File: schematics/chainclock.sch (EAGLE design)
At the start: 19 parts, among them SW1 ROTARTY_ENCODER

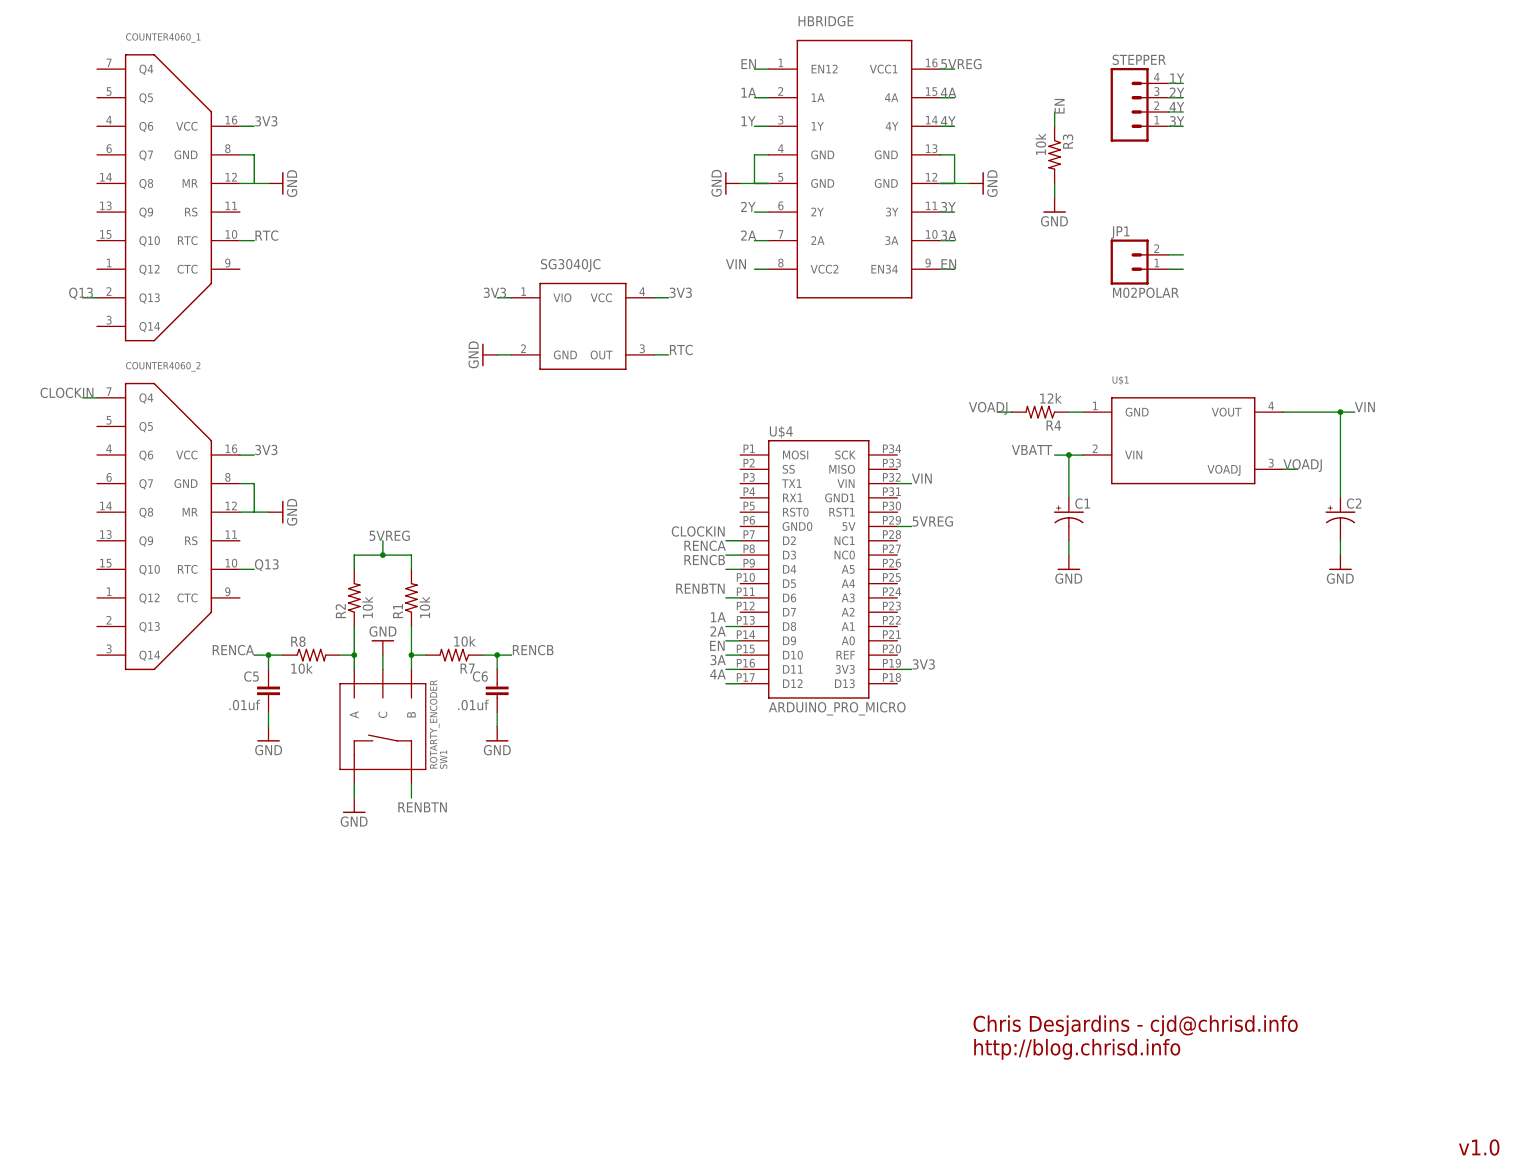
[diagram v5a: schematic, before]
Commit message: Move encoder off board
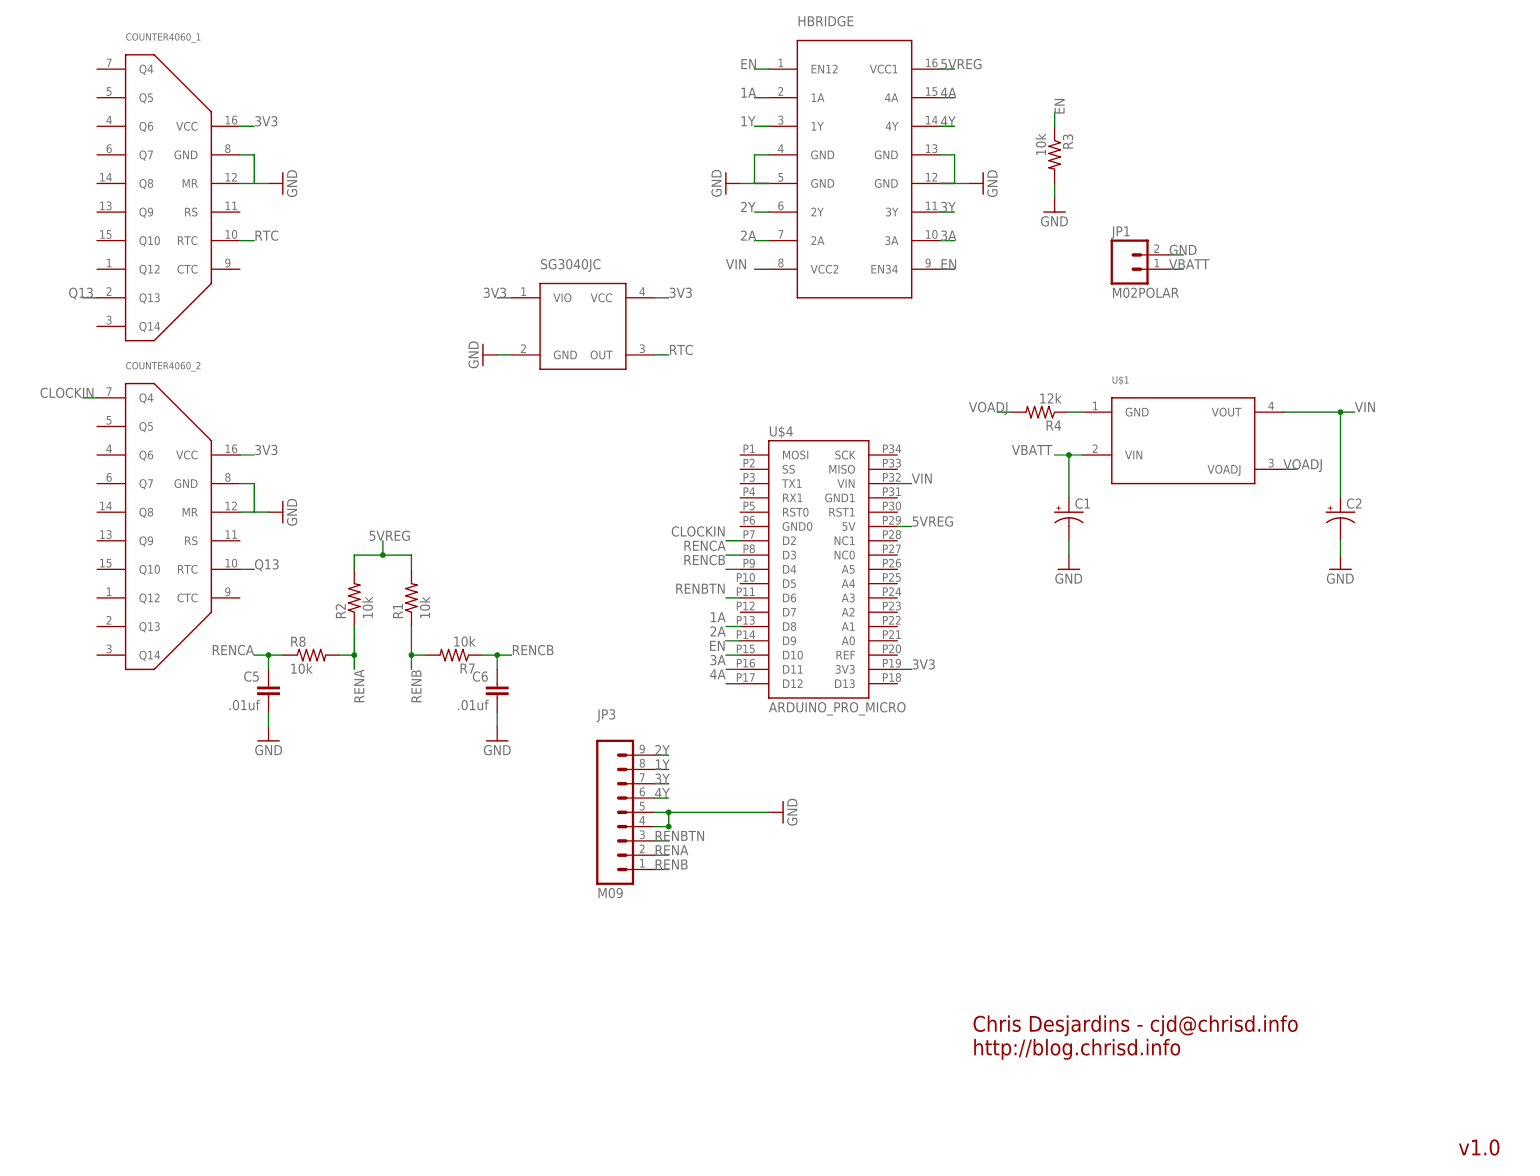
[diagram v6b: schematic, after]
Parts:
- removed STEPPER: (no value), SparkFun-Connectors:M04PTH
- removed SW1: ROTARTY_ENCODER, SparkFun-Electromechanical:ROTARTY_ENCODER
- added JP3: M09, SparkFun-Connectors:M09
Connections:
- removed net N$2: R1.1, R7.2, SW1.B
- removed net N$5: R2.1, R8.2, SW1.A
- new net RENA: JP3.2, R2.1, R8.2
- new net RENB: JP3.1, R1.1, R7.2
- net 1Y: now also JP3.8; no longer STEPPER.4
- net 2Y: now also JP3.9; no longer STEPPER.3
- net 3Y: now also JP3.7; no longer STEPPER.1
- net 4Y: now also JP3.6; no longer STEPPER.2
- net GND: now also JP3.4, JP3.5; no longer SW1.C, SW1.SW-
- net RENBTN: now also JP3.3; no longer SW1.SW+
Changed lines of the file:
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@@
 <part name="GND3" library="SparkFun-Aesthetics" deviceset="GND" device=""/>
 <part name="GND4" library="SparkFun-Aesthetics" deviceset="GND" device=""/>
-<part name="STEPPER" library="SparkFun-Connectors" deviceset="M04" device="PTH"/>
 <part name="R3" library="SparkFun-Resistors" deviceset="RESISTOR" device="EZ" value="10k"/>
 <part name="GND5" library="SparkFun-Aesthetics" deviceset="GND" device=""/>
 <part name="FRAME1" library="frames" deviceset="FRAME_A_L" device=""/>
-<part name="SW1" library="SparkFun-Electromechanical" deviceset="ROTARTY_ENCODER" device=""/>
-<part name="GND7" library="SparkFun-Aesthetics" deviceset="GND" device=""/>
 <part name="C5" library="SparkFun-Capacitors" deviceset="CAP" device="KIT" value=".01uf"/>
 <part name="C6" library="SparkFun-Capacitors" deviceset="CAP" device="KIT" value=".01uf"/>
 <part name="GND10" library="SparkFun-Aesthetics" deviceset="GND" device=""/>
 <part name="GND11" library="SparkFun-Aesthetics" deviceset="GND" device=""/>
-<part name="GND12" library="SparkFun-Aesthetics" deviceset="GND" device=""/>
 <part name="GND1" library="SparkFun-Aesthetics" deviceset="GND" device=""/>
 <part name="SG3040JC" library="desjardins" deviceset="SG30XX" device="JC"/>
@@
 <part name="COUNTER4060_2" library="desjardins" deviceset="4060" device="SOIC16"/>
 <part name="GND2" library="SparkFun-Aesthetics" deviceset="GND" device=""/>
+<part name="JP3" library="SparkFun-Connectors" deviceset="M09" device=""/>
+<part name="GND14" library="SparkFun-Aesthetics" deviceset="GND" device=""/>
 </parts>
 <sheets>
@@
 <instance part="GND3" gate="1" x="132.08" y="180.34" rot="R270"/>
 <instance part="GND4" gate="1" x="177.8" y="180.34" rot="R90"/>
-<instance part="STEPPER" gate="G$1" x="205.74" y="193.04"/>
 <instance part="R3" gate="G$1" x="190.5" y="185.42" rot="R270"/>
 <instance part="GND5" gate="1" x="190.5" y="175.26"/>
 <instance part="FRAME1" gate="G$1" x="0" y="0"/>
 <instance part="FRAME1" gate="G$2" x="172.72" y="0"/>
-<instance part="SW1" gate="G$1" x="71.12" y="83.82" rot="MR90"/>
-<instance part="GND7" gate="1" x="71.12" y="99.06" rot="R180"/>
 <instance part="C5" gate="G$1" x="50.8" y="88.9" rot="MR0"/>
 <instance part="C6" gate="G$1" x="91.44" y="88.9" rot="MR0"/>
 <instance part="GND10" gate="1" x="91.44" y="81.28" rot="MR0"/>
 <instance part="GND11" gate="1" x="50.8" y="81.28" rot="MR0"/>
-<instance part="GND12" gate="1" x="66.04" y="68.58"/>
 <instance part="GND1" gate="1" x="88.9" y="149.86" rot="R270"/>
 <instance part="SG3040JC" gate="G$1" x="106.68" y="154.94"/>
@@
 <instance part="COUNTER4060_2" gate="G$1" x="33.02" y="119.38"/>
 <instance part="GND2" gate="1" x="53.34" y="121.92" rot="R90"/>
+<instance part="JP3" gate="G$1" x="109.22" y="68.58"/>
+<instance part="GND14" gate="1" x="142.24" y="68.58" rot="MR270"/>
 </instances>
 <busses>
@@
 </segment>
 <segment>
-<pinref part="SW1" gate="G$1" pin="C"/>
-<wire x1="71.12" y1="93.98" x2="71.12" y2="96.52" width="0.1524" layer="91"/>
-<pinref part="GND7" gate="1" pin="GND"/>
-</segment>
-<segment>
 <pinref part="C6" gate="G$1" pin="2"/>
 <wire x1="91.44" y1="86.36" x2="91.44" y2="83.82" width="0.1524" layer="91"/>
@@
 </segment>
 <segment>
-<pinref part="SW1" gate="G$1" pin="SW-"/>
-<wire x1="66.04" y1="73.66" x2="66.04" y2="71.12" width="0.1524" layer="91"/>
-<pinref part="GND12" gate="1" pin="GND"/>
-</segment>
-<segment>
 <wire x1="93.98" y1="149.86" x2="91.44" y2="149.86" width="0.1524" layer="91"/>
 <pinref part="GND1" gate="1" pin="GND"/>
@@
 <pinref part="JP1" gate="G$1" pin="2"/>
 <wire x1="210.82" y1="167.64" x2="213.36" y2="167.64" width="0.1524" layer="91"/>
+<label x="210.82" y="167.64" size="1.778" layer="95"/>
 </segment>
 <segment>
@@
 <pinref part="GND2" gate="1" pin="GND"/>
 </segment>
+<segment>
+<pinref part="JP3" gate="G$1" pin="4"/>
+<wire x1="119.38" y1="66.04" x2="121.92" y2="66.04" width="0.1524" layer="91"/>
+<wire x1="121.92" y1="66.04" x2="121.92" y2="68.58" width="0.1524" layer="91"/>
+<pinref part="JP3" gate="G$1" pin="5"/>
+<wire x1="119.38" y1="68.58" x2="121.92" y2="68.58" width="0.1524" layer="91"/>
+<junction x="121.92" y="68.58"/>
+<wire x1="121.92" y1="68.58" x2="139.7" y2="68.58" width="0.1524" layer="91"/>
+<junction x="121.92" y="66.04"/>
+<pinref part="GND14" gate="1" pin="GND"/>
+</segment>
 </net>
 <net name="CLOCKIN" class="0">
@@
 </segment>
 <segment>
-<pinref part="STEPPER" gate="G$1" pin="4"/>
-<wire x1="210.82" y1="198.12" x2="213.36" y2="198.12" width="0.1524" layer="91"/>
-<label x="210.82" y="198.12" size="1.778" layer="95"/>
+<pinref part="JP3" gate="G$1" pin="8"/>
+<wire x1="119.38" y1="76.2" x2="121.92" y2="76.2" width="0.1524" layer="91"/>
+<label x="119.38" y="76.2" size="1.778" layer="95"/>
 </segment>
 </net>
@@
 </segment>
 <segment>
-<pinref part="STEPPER" gate="G$1" pin="2"/>
-<wire x1="210.82" y1="193.04" x2="213.36" y2="193.04" width="0.1524" layer="91"/>
-<label x="210.82" y="193.04" size="1.778" layer="95"/>
+<pinref part="JP3" gate="G$1" pin="6"/>
+<wire x1="119.38" y1="71.12" x2="121.92" y2="71.12" width="0.1524" layer="91"/>
+<label x="119.38" y="71.12" size="1.778" layer="95"/>
 </segment>
 </net>
@@
 </segment>
 <segment>
-<pinref part="STEPPER" gate="G$1" pin="1"/>
-<wire x1="210.82" y1="190.5" x2="213.36" y2="190.5" width="0.1524" layer="91"/>
-<label x="210.82" y="190.5" size="1.778" layer="95"/>
+<pinref part="JP3" gate="G$1" pin="7"/>
+<wire x1="119.38" y1="73.66" x2="121.92" y2="73.66" width="0.1524" layer="91"/>
+<label x="119.38" y="73.66" size="1.778" layer="95"/>
 </segment>
 </net>
@@
 </segment>
 <segment>
-<pinref part="STEPPER" gate="G$1" pin="3"/>
-<wire x1="210.82" y1="195.58" x2="213.36" y2="195.58" width="0.1524" layer="91"/>
-<label x="210.82" y="195.58" size="1.778" layer="95"/>
+<pinref part="JP3" gate="G$1" pin="9"/>
+<wire x1="119.38" y1="78.74" x2="121.92" y2="78.74" width="0.1524" layer="91"/>
+<label x="119.38" y="78.74" size="1.778" layer="95"/>
 </segment>
 </net>
@@
 </segment>
 </net>
-<net name="N$2" class="0">
-<segment>
-<pinref part="SW1" gate="G$1" pin="B"/>
+<net name="RENB" class="0">
+<segment>
 <wire x1="76.2" y1="93.98" x2="76.2" y2="96.52" width="0.1524" layer="91"/>
 <pinref part="R1" gate="G$1" pin="1"/>
@@
 <wire x1="76.2" y1="96.52" x2="78.74" y2="96.52" width="0.1524" layer="91"/>
 <junction x="76.2" y="96.52"/>
-</segment>
-</net>
-<net name="N$5" class="0">
-<segment>
-<pinref part="SW1" gate="G$1" pin="A"/>
+<label x="76.2" y="93.98" size="1.778" layer="95" rot="R270"/>
+</segment>
+<segment>
+<pinref part="JP3" gate="G$1" pin="1"/>
+<wire x1="119.38" y1="58.42" x2="121.92" y2="58.42" width="0.1524" layer="91"/>
+<label x="119.38" y="58.42" size="1.778" layer="95"/>
+</segment>
+</net>
+<net name="RENA" class="0">
+<segment>
 <wire x1="66.04" y1="93.98" x2="66.04" y2="96.52" width="0.1524" layer="91"/>
 <wire x1="66.04" y1="96.52" x2="63.5" y2="96.52" width="0.1524" layer="91"/>
@@
 <pinref part="R8" gate="G$1" pin="2"/>
 <pinref part="R2" gate="G$1" pin="1"/>
+<label x="66.04" y="93.98" size="1.778" layer="95" rot="R270"/>
+</segment>
+<segment>
+<pinref part="JP3" gate="G$1" pin="2"/>
+<wire x1="119.38" y1="60.96" x2="121.92" y2="60.96" width="0.1524" layer="91"/>
+<label x="119.38" y="60.96" size="1.778" layer="95"/>
 </segment>
 </net>
 <net name="RENBTN" class="0">
-<segment>
-<pinref part="SW1" gate="G$1" pin="SW+"/>
-<wire x1="76.2" y1="73.66" x2="76.2" y2="71.12" width="0.1524" layer="91"/>
-<label x="73.66" y="68.58" size="1.778" layer="95"/>
-</segment>
 <segment>
 <pinref part="U$4" gate="G$1" pin="D6"/>
 <wire x1="134.62" y1="106.68" x2="132.08" y2="106.68" width="0.1524" layer="91"/>
 <label x="132.08" y="109.22" size="1.778" layer="95" rot="R180"/>
+</segment>
+<segment>
+<pinref part="JP3" gate="G$1" pin="3"/>
+<wire x1="119.38" y1="63.5" x2="121.92" y2="63.5" width="0.1524" layer="91"/>
+<label x="119.38" y="63.5" size="1.778" layer="95"/>
 </segment>
 </net>
@@
 <pinref part="JP1" gate="G$1" pin="1"/>
 <wire x1="210.82" y1="165.1" x2="213.36" y2="165.1" width="0.1524" layer="91"/>
-</segment>
-</net>
+<label x="210.82" y="165.1" size="1.778" layer="95"/>
+</segment>
+</net>

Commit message: Updates to chainlock
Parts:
- removed C1, C2: (no value), SparkFun-Capacitors:CAP_POLPTH1
- added C3, C4: 100uf, SparkFun-Capacitors:0.1UF-50V-20%(PTH)KIT-EZ
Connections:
- net GND: now also C3.2, C4.2; no longer C1.-, C2.-
- net VBATT: now also C3.1; no longer C1.+
- net VIN: now also C4.1; no longer C2.+
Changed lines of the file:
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@@
 <part name="U$4" library="ChrisD" deviceset="ARDUINO_PRO_MICRO" device=""/>
 <part name="U$1" library="desjardins" deviceset="PTN0405C" device=""/>
-<part name="C1" library="SparkFun-Capacitors" deviceset="CAP_POL" device="PTH1"/>
-<part name="C2" library="SparkFun-Capacitors" deviceset="CAP_POL" device="PTH1"/>
 <part name="R4" library="SparkFun-Resistors" deviceset="RESISTOR" device="EZ" value="12k"/>
 <part name="GND6" library="SparkFun-Aesthetics" deviceset="GND" device=""/>
@@
 <part name="JP3" library="SparkFun-Connectors" deviceset="M09" device=""/>
 <part name="GND14" library="SparkFun-Aesthetics" deviceset="GND" device=""/>
+<part name="C3" library="SparkFun-Capacitors" deviceset="0.1UF-50V-20%(PTH)" device="KIT-EZ" value="100uf"/>
+<part name="C4" library="SparkFun-Capacitors" deviceset="0.1UF-50V-20%(PTH)" device="KIT-EZ" value="100uf"/>
 </parts>
 <sheets>
@@
 <instance part="U$4" gate="G$1" x="147.32" y="116.84"/>
 <instance part="U$1" gate="G$1" x="213.36" y="134.62"/>
-<instance part="C1" gate="G$1" x="193.04" y="121.92"/>
-<instance part="C2" gate="G$1" x="241.3" y="121.92"/>
 <instance part="R4" gate="G$1" x="187.96" y="139.7" rot="R180"/>
 <instance part="GND6" gate="1" x="241.3" y="111.76"/>
@@
 <instance part="JP3" gate="G$1" x="109.22" y="68.58"/>
 <instance part="GND14" gate="1" x="142.24" y="68.58" rot="MR270"/>
+<instance part="C3" gate="G$1" x="193.04" y="119.38"/>
+<instance part="C4" gate="G$1" x="241.3" y="119.38"/>
 </instances>
 <busses>
@@
 </segment>
 <segment>
-<pinref part="C2" gate="G$1" pin="-"/>
 <wire x1="241.3" y1="116.84" x2="241.3" y2="114.3" width="0.1524" layer="91"/>
 <pinref part="GND6" gate="1" pin="GND"/>
-</segment>
-<segment>
-<pinref part="C1" gate="G$1" pin="-"/>
+<pinref part="C4" gate="G$1" pin="2"/>
+</segment>
+<segment>
 <wire x1="193.04" y1="116.84" x2="193.04" y2="114.3" width="0.1524" layer="91"/>
 <pinref part="GND8" gate="1" pin="GND"/>
+<pinref part="C3" gate="G$1" pin="2"/>
 </segment>
 <segment>
@@
 <junction x="241.3" y="139.7"/>
 <label x="243.84" y="139.7" size="1.778" layer="95"/>
-<pinref part="C2" gate="G$1" pin="+"/>
+<pinref part="C4" gate="G$1" pin="1"/>
 </segment>
 </net>
@@
 <wire x1="193.04" y1="132.08" x2="190.5" y2="132.08" width="0.1524" layer="91"/>
 <wire x1="193.04" y1="132.08" x2="193.04" y2="124.46" width="0.1524" layer="91"/>
-<pinref part="C1" gate="G$1" pin="+"/>
 <junction x="193.04" y="132.08"/>
 <label x="182.88" y="132.08" size="1.778" layer="95"/>
-</segment>
-<segment>
+<pinref part="C3" gate="G$1" pin="1"/>
+</segment>
+<segment>

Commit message: Originize the routin
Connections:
- net GND: now also U$4.GND0, U$4.GND1
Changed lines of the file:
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@@
 <part name="C3" library="SparkFun-Capacitors" deviceset="0.1UF-50V-20%(PTH)" device="KIT-EZ" value="100uf"/>
 <part name="C4" library="SparkFun-Capacitors" deviceset="0.1UF-50V-20%(PTH)" device="KIT-EZ" value="100uf"/>
+<part name="GND7" library="SparkFun-Aesthetics" deviceset="GND" device=""/>
+<part name="GND12" library="SparkFun-Aesthetics" deviceset="GND" device=""/>
 </parts>
 <sheets>
@@
 <instance part="C3" gate="G$1" x="193.04" y="119.38"/>
 <instance part="C4" gate="G$1" x="241.3" y="119.38"/>
+<instance part="GND7" gate="1" x="119.38" y="119.38" rot="MR90"/>
+<instance part="GND12" gate="1" x="167.64" y="124.46" rot="MR270"/>
 </instances>
 <busses>
@@
 <pinref part="GND14" gate="1" pin="GND"/>
 </segment>
+<segment>
+<pinref part="U$4" gate="G$1" pin="GND0"/>
+<wire x1="134.62" y1="119.38" x2="121.92" y2="119.38" width="0.1524" layer="91"/>
+<pinref part="GND7" gate="1" pin="GND"/>
+</segment>
+<segment>
+<pinref part="U$4" gate="G$1" pin="GND1"/>
+<wire x1="162.56" y1="124.46" x2="165.1" y2="124.46" width="0.1524" layer="91"/>
+<pinref part="GND12" gate="1" pin="GND"/>
+</segment>
 </net>
